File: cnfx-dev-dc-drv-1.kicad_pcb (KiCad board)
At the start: 2 copper layers, 51.3 x 51.3 mm, 66 parts, among them J1 Conn_01x03, J2 TC2030, J3 Conn_01x02, J4 Conn_01x02, J5 Conn_01x04_Pin, J6 Conn_01x02, J7 Conn_01x02, SW1 SW_Push, SW2 SW_Push, SW3 SW_Push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

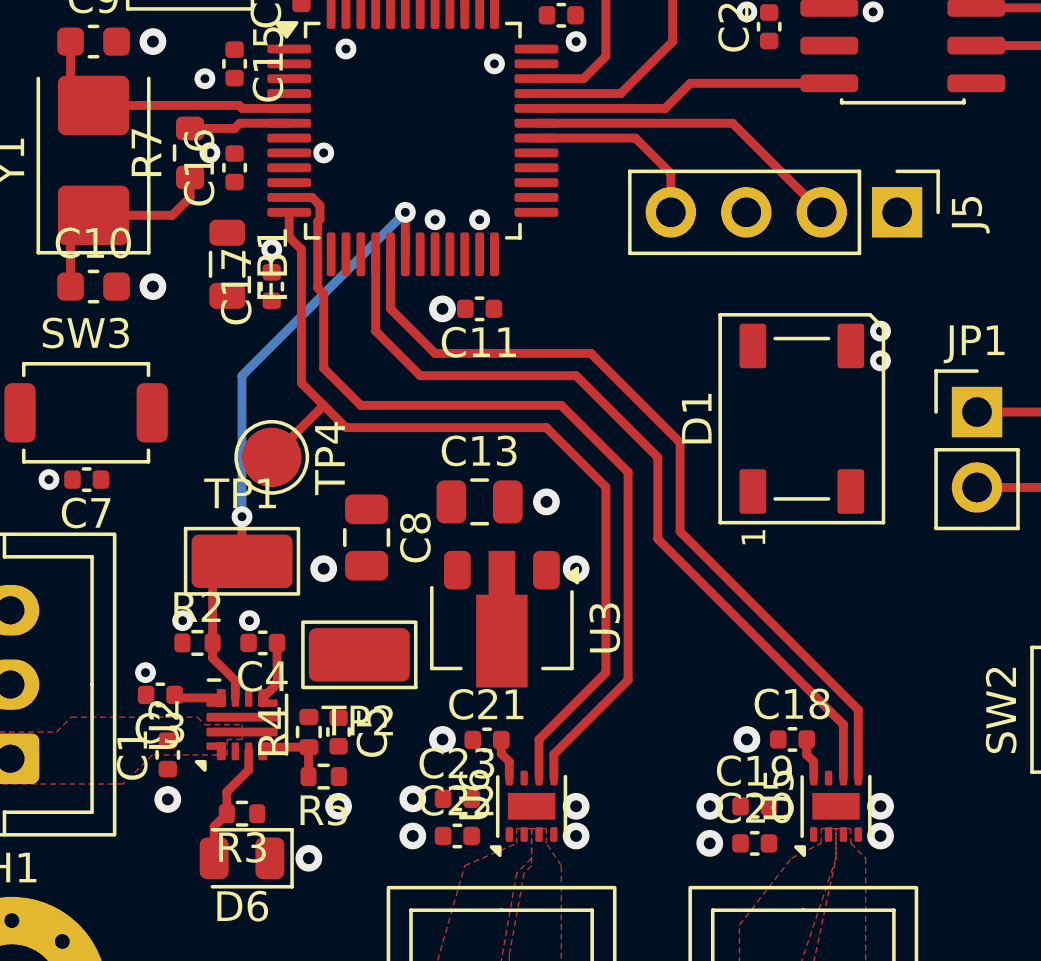
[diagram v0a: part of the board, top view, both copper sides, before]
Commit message: pcb: add dc drivers sleep pin routing
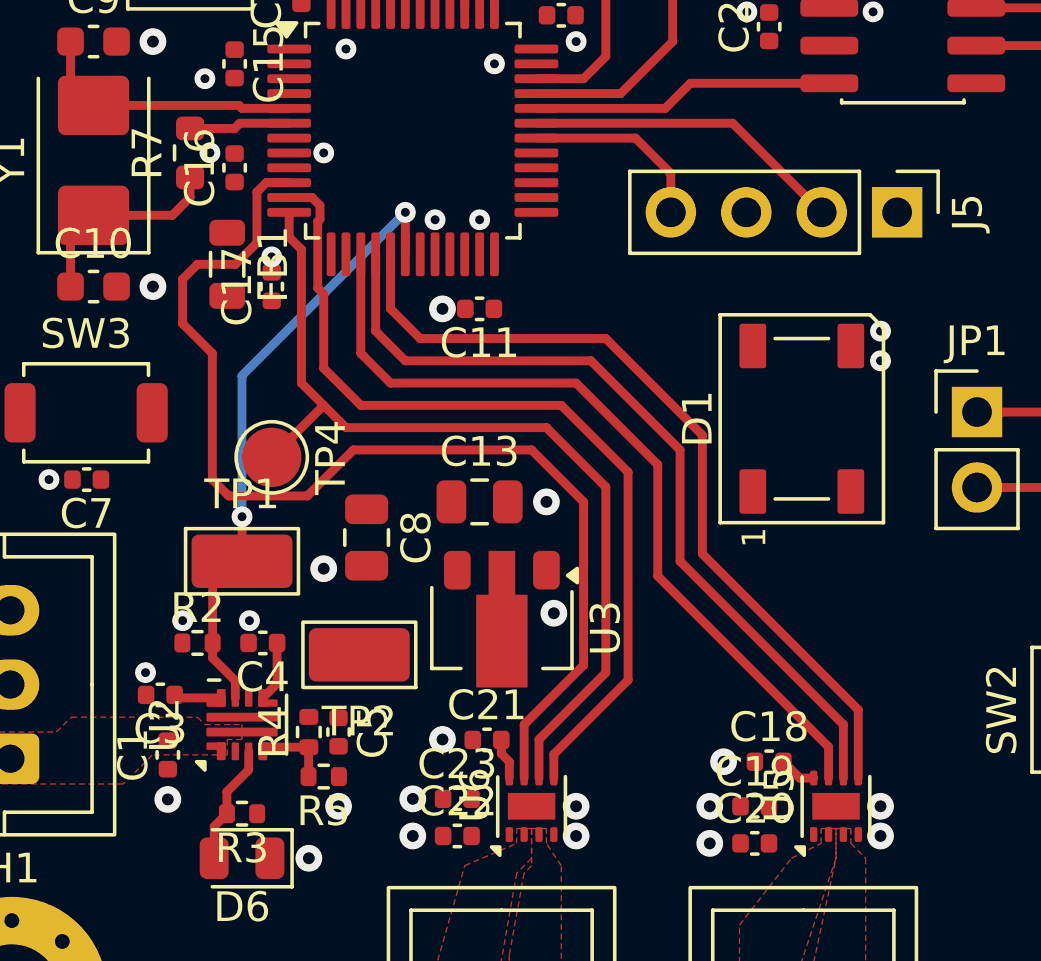
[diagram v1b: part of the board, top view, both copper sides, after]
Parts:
- moved C18 1.09 mm to (125.5, 92.2)
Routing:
- net /DC Driver 2/~{SLEEP}: track 0.00 -> 37.3 mm
- net /DC Driver/~{SLEEP}: track 0.00 -> 27.8 mm
- net /DC Driver/IN2: track 27.2 -> 27.8 mm
- net /DC Driver/IN1: track 27.2 -> 27.8 mm
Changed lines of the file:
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@@
 	(footprint "Capacitor_SMD:C_0402_1005Metric"
 		(layer "F.Cu")
-		(at 126.285 91.5)
+		(at 125.5 92.25)
 		(descr "Capacitor SMD 0402 (1005 Metric), square (rectangular) end terminal, IPC-7351 nominal, (Body size source: IPC-SM-782 page 76, https://www.pcb-3d.com/wordpress/wp-content/uploads/ipc-sm-782a_amendment_1_and_2.pdf)")
 		(tags "capacitor")
@@
 	)
 	(via
-		(at 124.75 91.5)
+		(at 123.965 92.25)
 		(size 0.9)
 		(drill 0.4)
@@
 	)
 	(via
-		(at 119 85.75)
+		(at 118.25 87.25)
 		(size 0.9)
 		(drill 0.4)
@@
 	)
 	(via
-		(at 108.75 75)
+		(at 108.75 75.25)
 		(size 0.7)
 		(drill 0.3)
@@
 	)
 	(segment
-		(start 126.765 91.5)
-		(end 126.765 92.015)
-		(width 0.3)
-		(layer "F.Cu")
-		(net "+3V3")
-	)
-	(segment
 		(start 116.75 92.25)
 		(end 116.75 92.8)
@@
 	)
 	(segment
-		(start 126.765 92.015)
-		(end 127 92.25)
+		(start 116.48 91.515)
+		(end 116.48 91.98)
 		(width 0.3)
 		(layer "F.Cu")
@@
 	)
 	(segment
-		(start 127 92.25)
-		(end 127 92.8)
+		(start 111 57.5)
+		(end 111.5 57)
 		(width 0.3)
 		(layer "F.Cu")
@@
 	)
 	(segment
-		(start 116.48 91.515)
-		(end 116.48 91.98)
+		(start 126.53 92.8)
+		(end 125.98 92.25)
 		(width 0.3)
 		(layer "F.Cu")
@@
 	)
 	(segment
-		(start 111 57.5)
-		(end 111.5 57)
+		(start 111.5 57)
+		(end 113.5 57)
 		(width 0.3)
 		(layer "F.Cu")
@@
 	)
 	(segment
-		(start 111.5 57)
-		(end 113.5 57)
+		(start 111 58.23)
+		(end 111 57.5)
 		(width 0.3)
 		(layer "F.Cu")
@@
 	)
 	(segment
-		(start 111 58.23)
-		(end 111 57.5)
+		(start 127 92.8)
+		(end 126.53 92.8)
 		(width 0.3)
 		(layer "F.Cu")
@@
 	(segment
 		(start 112.75 77)
-		(end 114.25 78.5)
+		(end 113.75 78)
 		(width 0.3)
 		(layer "F.Cu")
@@
 	)
 	(segment
-		(start 122.5 81.5)
-		(end 122.5 84.5)
+		(start 123.25 85.25)
+		(end 128.5 90.5)
 		(width 0.3)
 		(layer "F.Cu")
@@
 	)
 	(segment
-		(start 122.5 84.5)
-		(end 128.5 90.5)
+		(start 112.75 75.1625)
+		(end 112.75 77)
 		(width 0.3)
 		(layer "F.Cu")
@@
 	)
 	(segment
-		(start 119.5 78.5)
-		(end 122.5 81.5)
+		(start 113.75 78)
+		(end 120 78)
 		(width 0.3)
 		(layer "F.Cu")
@@
 	)
 	(segment
-		(start 112.75 75.1625)
-		(end 112.75 77)
+		(start 128.5 90.5)
+		(end 128.5 92.8)
 		(width 0.3)
 		(layer "F.Cu")
@@
 	)
 	(segment
-		(start 114.25 78.5)
-		(end 119.5 78.5)
+		(start 120 78)
+		(end 123.25 81.25)
 		(width 0.3)
 		(layer "F.Cu")
@@
 	)
 	(segment
-		(start 128.5 90.5)
-		(end 128.5 92.8)
+		(start 123.25 81.25)
+		(end 123.25 85.25)
 		(width 0.3)
 		(layer "F.Cu")
@@
 	)
 	(segment
+		(start 127.5 91.75)
+		(end 127.5 92.8)
+		(width 0.3)
+		(layer "F.Cu")
+		(net "/DC Driver/~{SLEEP}")
+	)
+	(segment
+		(start 111.75 75.1625)
+		(end 111.75 78.5)
+		(width 0.3)
+		(layer "F.Cu")
+		(net "/DC Driver/~{SLEEP}")
+	)
+	(segment
+		(start 119 79.5)
+		(end 121.75 82.25)
+		(width 0.3)
+		(layer "F.Cu")
+		(net "/DC Driver/~{SLEEP}")
+	)
+	(segment
+		(start 121.75 82.25)
+		(end 121.75 86)
+		(width 0.3)
+		(layer "F.Cu")
+		(net "/DC Driver/~{SLEEP}")
+	)
+	(segment
+		(start 121.75 86)
+		(end 127.5 91.75)
+		(width 0.3)
+		(layer "F.Cu")
+		(net "/DC Driver/~{SLEEP}")
+	)
+	(segment
+		(start 111.75 78.5)
+		(end 112.75 79.5)
+		(width 0.3)
+		(layer "F.Cu")
+		(net "/DC Driver/~{SLEEP}")
+	)
+	(segment
+		(start 112.75 79.5)
+		(end 119 79.5)
+		(width 0.3)
+		(layer "F.Cu")
+		(net "/DC Driver/~{SLEEP}")
+	)
+	(segment
 		(start 122.25 66.5)
 		(end 123.155 65.595)
@@
 	)
 	(segment
-		(start 112.25 77.75)
-		(end 112.25 75.1625)
+		(start 105.75 76)
+		(end 106.25 75.5)
+		(width 0.3)
+		(layer "F.Cu")
+		(net "/DC Driver 2/~{SLEEP}")
+	)
+	(segment
+		(start 106.75 82.75)
+		(end 106.75 78.5)
+		(width 0.3)
+		(layer "F.Cu")
+		(net "/DC Driver 2/~{SLEEP}")
+	)
+	(segment
+		(start 107.527186 75.5)
+		(end 108.25 74.777186)
+		(width 0.3)
+		(layer "F.Cu")
+		(net "/DC Driver 2/~{SLEEP}")
+	)
+	(segment
+		(start 108.56759 72.75)
+		(end 109.3375 72.75)
+		(width 0.3)
+		(layer "F.Cu")
+		(net "/DC Driver 2/~{SLEEP}")
+	)
+	(segment
+		(start 119.25 89)
+		(end 119.25 83.5)
+		(width 0.3)
+		(layer "F.Cu")
+		(net "/DC Driver 2/~{SLEEP}")
+	)
+	(segment
+		(start 111.5 81.75)
+		(end 109.95 83.3)
+		(width 0.3)
+		(layer "F.Cu")
+		(net "/DC Driver 2/~{SLEEP}")
+	)
+	(segment
+		(start 106.25 75.5)
+		(end 107.527186 75.5)
+		(width 0.3)
+		(layer "F.Cu")
+		(net "/DC Driver 2/~{SLEEP}")
+	)
+	(segment
+		(start 119.25 83.5)
+		(end 117.5 81.75)
+		(width 0.3)
+		(layer "F.Cu")
+		(net "/DC Driver 2/~{SLEEP}")
+	)
+	(segment
+		(start 107.3 83.3)
+		(end 106.75 82.75)
+		(width 0.3)
+		(layer "F.Cu")
+		(net "/DC Driver 2/~{SLEEP}")
+	)
+	(segment
+		(start 117.5 81.75)
+		(end 111.5 81.75)
+		(width 0.3)
+		(layer "F.Cu")
+		(net "/DC Driver 2/~{SLEEP}")
+	)
+	(segment
+		(start 117.25 91)
+		(end 119.25 89)
+		(width 0.3)
+		(layer "F.Cu")
+		(net "/DC Driver 2/~{SLEEP}")
+	)
+	(segment
+		(start 117.25 92.8)
+		(end 117.25 91)
+		(width 0.3)
+		(layer "F.Cu")
+		(net "/DC Driver 2/~{SLEEP}")
+	)
+	(segment
+		(start 108.25 74.777186)
+		(end 108.25 73.06759)
+		(width 0.3)
+		(layer "F.Cu")
+		(net "/DC Driver 2/~{SLEEP}")
+	)
+	(segment
+		(start 108.25 73.06759)
+		(end 108.56759 72.75)
+		(width 0.3)
+		(layer "F.Cu")
+		(net "/DC Driver 2/~{SLEEP}")
+	)
+	(segment
+		(start 106.75 78.5)
+		(end 105.75 77.5)
+		(width 0.3)
+		(layer "F.Cu")
+		(net "/DC Driver 2/~{SLEEP}")
+	)
+	(segment
+		(start 109.95 83.3)
+		(end 107.3 83.3)
+		(width 0.3)
+		(layer "F.Cu")
+		(net "/DC Driver 2/~{SLEEP}")
+	)
+	(segment
+		(start 105.75 77.5)
+		(end 105.75 76)
+		(width 0.3)
+		(layer "F.Cu")
+		(net "/DC Driver 2/~{SLEEP}")
+	)
+	(segment
+		(start 122.5 81.75)
+		(end 119.5 78.75)
 		(width 0.3)
 		(layer "F.Cu")
@@
 	)
 	(segment
-		(start 121.75 84.75)
-		(end 121.75 82)
+		(start 112.25 77.75)
+		(end 112.25 75.1625)
 		(width 0.3)
 		(layer "F.Cu")
@@
 	)
 	(segment
-		(start 128 92.8)
-		(end 128 91)
+		(start 119.5 78.75)
+		(end 113.25 78.75)
 		(width 0.3)
 		(layer "F.Cu")
@@
 	)
 	(segment
-		(start 128 91)
-		(end 121.75 84.75)
+		(start 128 92.8)
+		(end 128 91)
 		(width 0.3)
 		(layer "F.Cu")
@@
 	)
 	(segment
-		(start 121.75 82)
-		(end 119 79.25)
+		(start 128 91)
+		(end 122.5 85.5)
 		(width 0.3)
 		(layer "F.Cu")
@@
 	)
 	(segment
-		(start 113.75 79.25)
+		(start 113.25 78.75)
 		(end 112.25 77.75)
 		(width 0.3)
@@
 	)
 	(segment
-		(start 119 79.25)
-		(end 113.75 79.25)
+		(start 122.5 85.5)
+		(end 122.5 81.75)
 		(width 0.3)
 		(layer "F.Cu")

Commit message: pcb: add +5V pwr routing
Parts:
- moved C8 1.13 mm to (112.8, 85.5), turned to 90 degrees
- moved C20 1.07 mm to (124.2, 94.2), turned to -90 degrees
- moved TP4 1.03 mm to (108.5, 81.0)
- moved C23 0.90 mm to (115.5, 94.2), turned to -90 degrees
- moved C7 0.75 mm to (101.8, 82.8)
- moved SW3 0.75 mm to (101.8, 80.5)
- moved C22 0.71 mm to (114.5, 94.2), turned to -90 degrees
- moved C19 0.55 mm to (125.2, 94.2), turned to -90 degrees
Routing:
- net +5V: track 0.00 -> 68.1 mm
- net +3V3: track 7.48 -> 9.86 mm
- net /DC Driver 2/~{SLEEP}: track 37.3 -> 36.8 mm
- added copper zone on F.Cu, net +5V

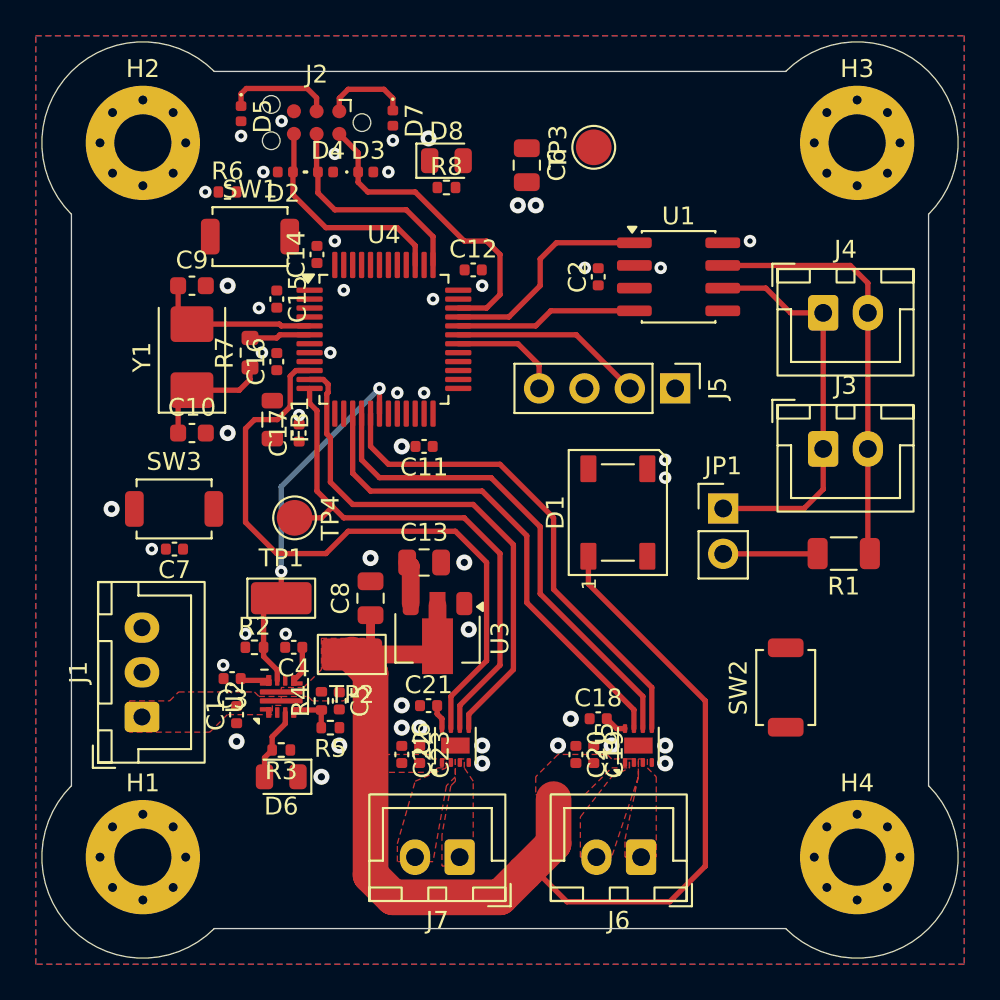
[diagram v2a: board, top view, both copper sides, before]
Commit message: pcb: add +3V3 pwr routing
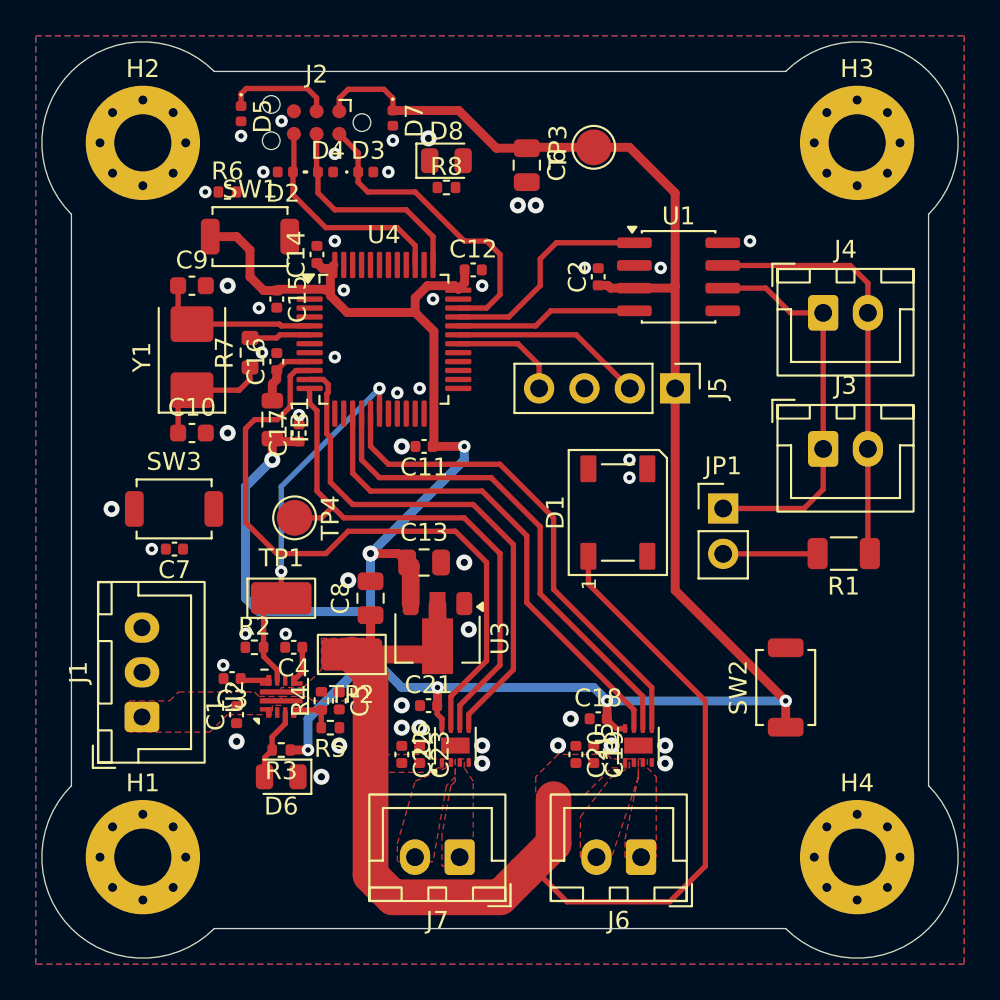
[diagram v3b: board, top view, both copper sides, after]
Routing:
- net +3V3: track 9.86 -> 164.4 mm, vias 0 -> 7
- net Net-(U4-VDDA): track 0.00 -> 3.85 mm

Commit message: pcb: add RGB and btns routing
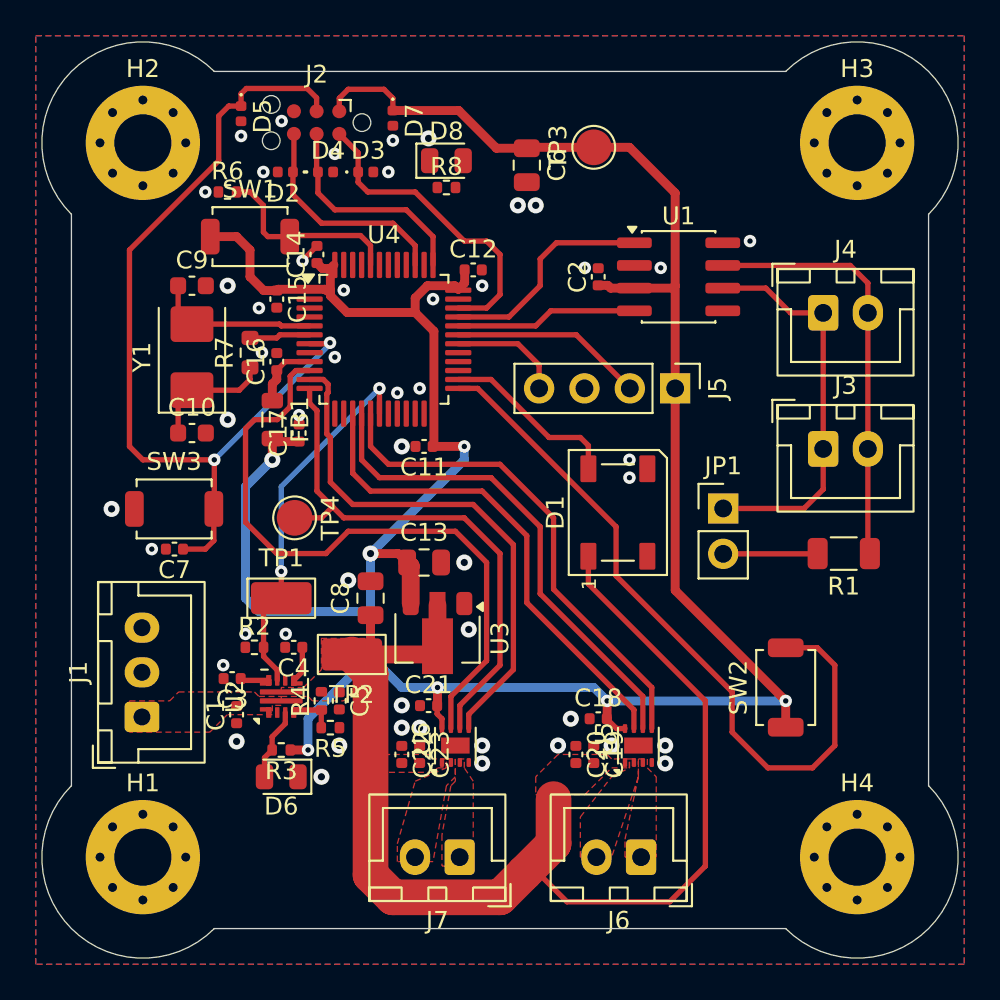
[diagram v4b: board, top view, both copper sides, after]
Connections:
- U4 pad 25: /RGB -> /BTN1
- U4 pad 26: unconnected-(U4-PB13-Pad26) -> /RGB
- U4 pad 41: /BTN1 -> unconnected-(U4-PB5-Pad41)
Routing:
- net /NRST: track 6.01 -> 50.0 mm, vias 0 -> 2
- net /BTN1: track 0.00 -> 41.0 mm
- net /BOOT: track 0.00 -> 10.8 mm
- net /RGB: track 0.00 -> 10.1 mm
- net GND: track 0.00 -> 1.17 mm
